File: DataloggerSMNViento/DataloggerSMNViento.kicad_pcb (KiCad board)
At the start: 2 copper layers, 85.7 x 137.2 mm, 37 parts, among them J1 Conn_01x01_Male, J2 Conn_01x01_Male, J3 Conn_01x01_Male, J4 Conn_01x01_Male, Q1 2N7000, Q2 2N7000, Q3 2N7000, U2 w5100_module

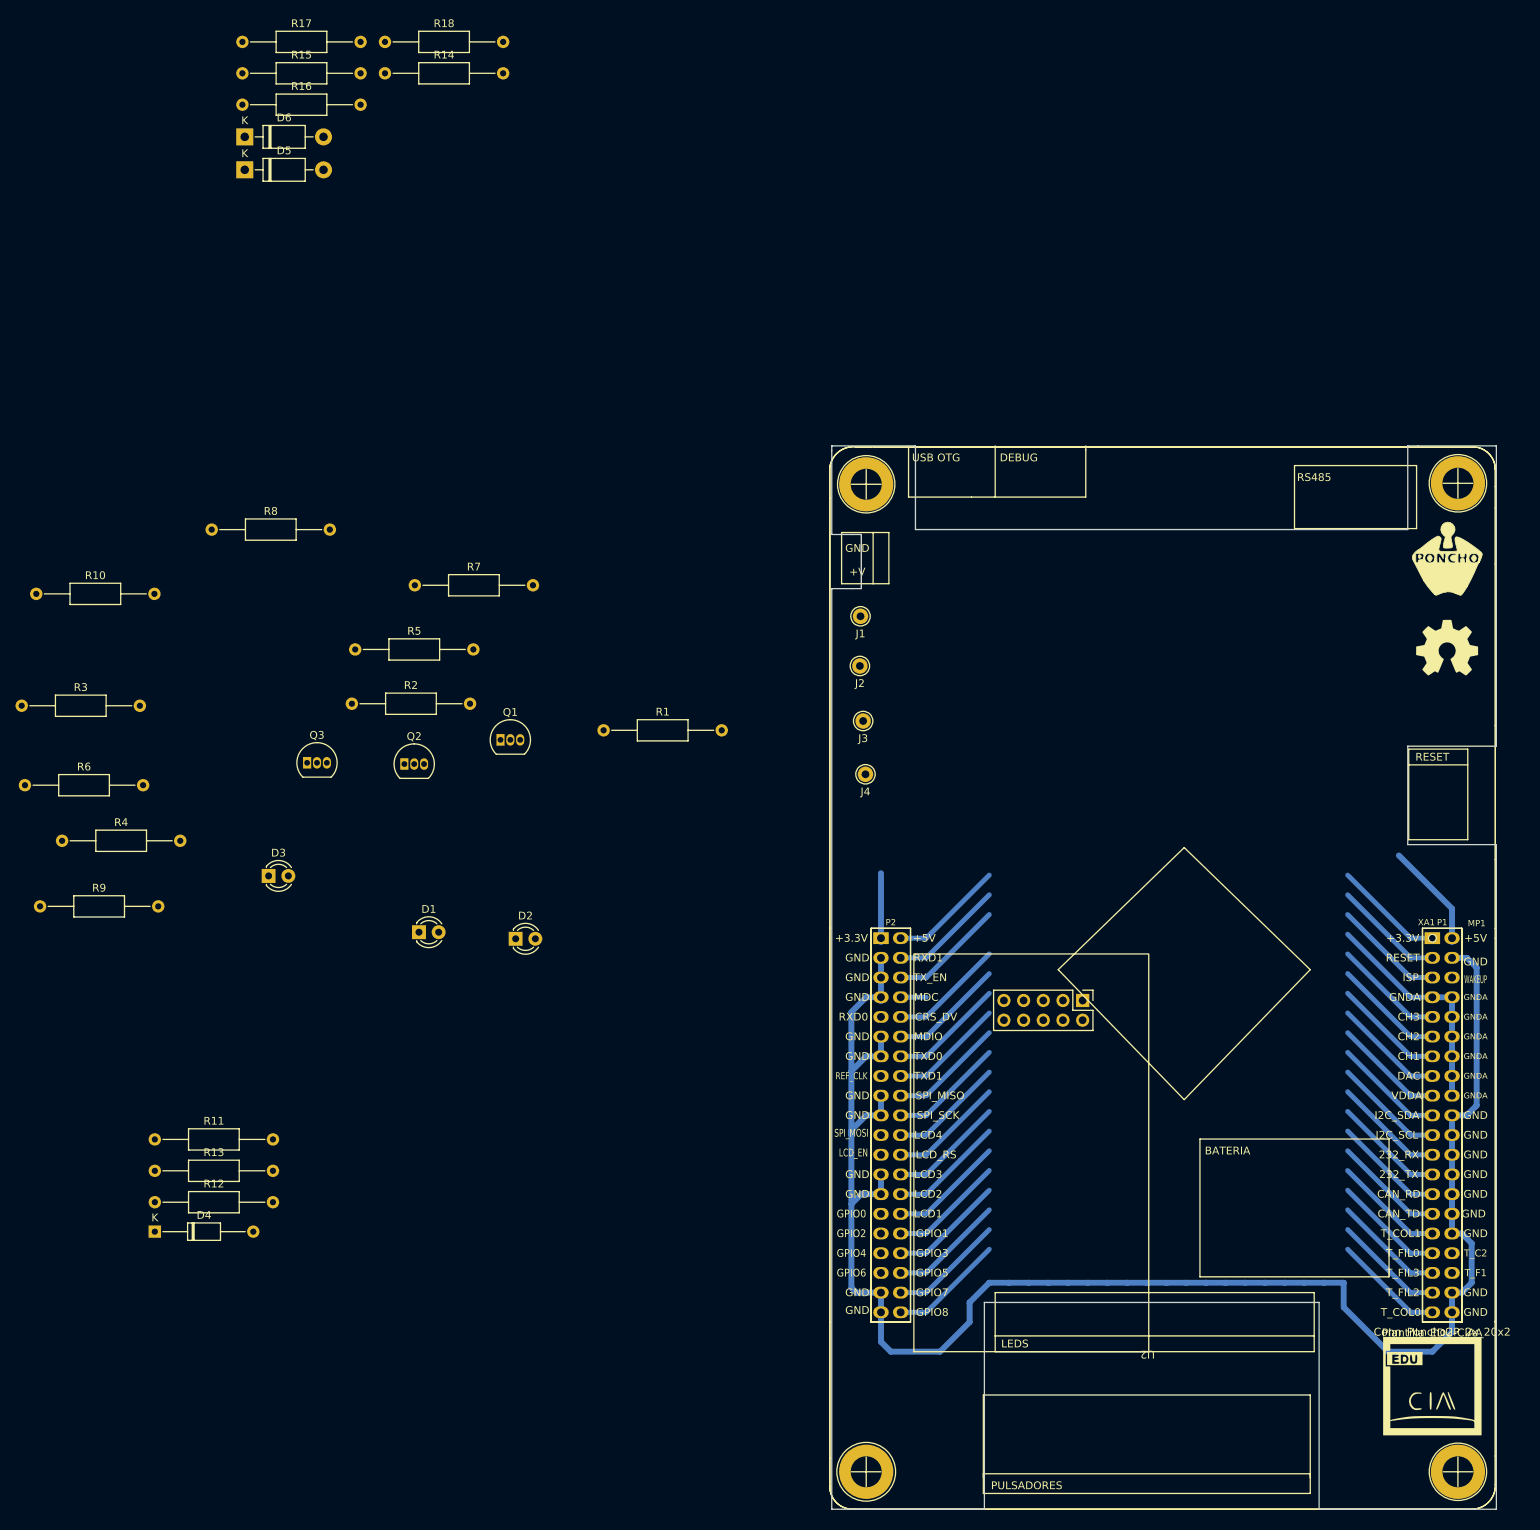
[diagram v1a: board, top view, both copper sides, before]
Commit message: Subo la version v1.0 del PCB del poncho de la tesis
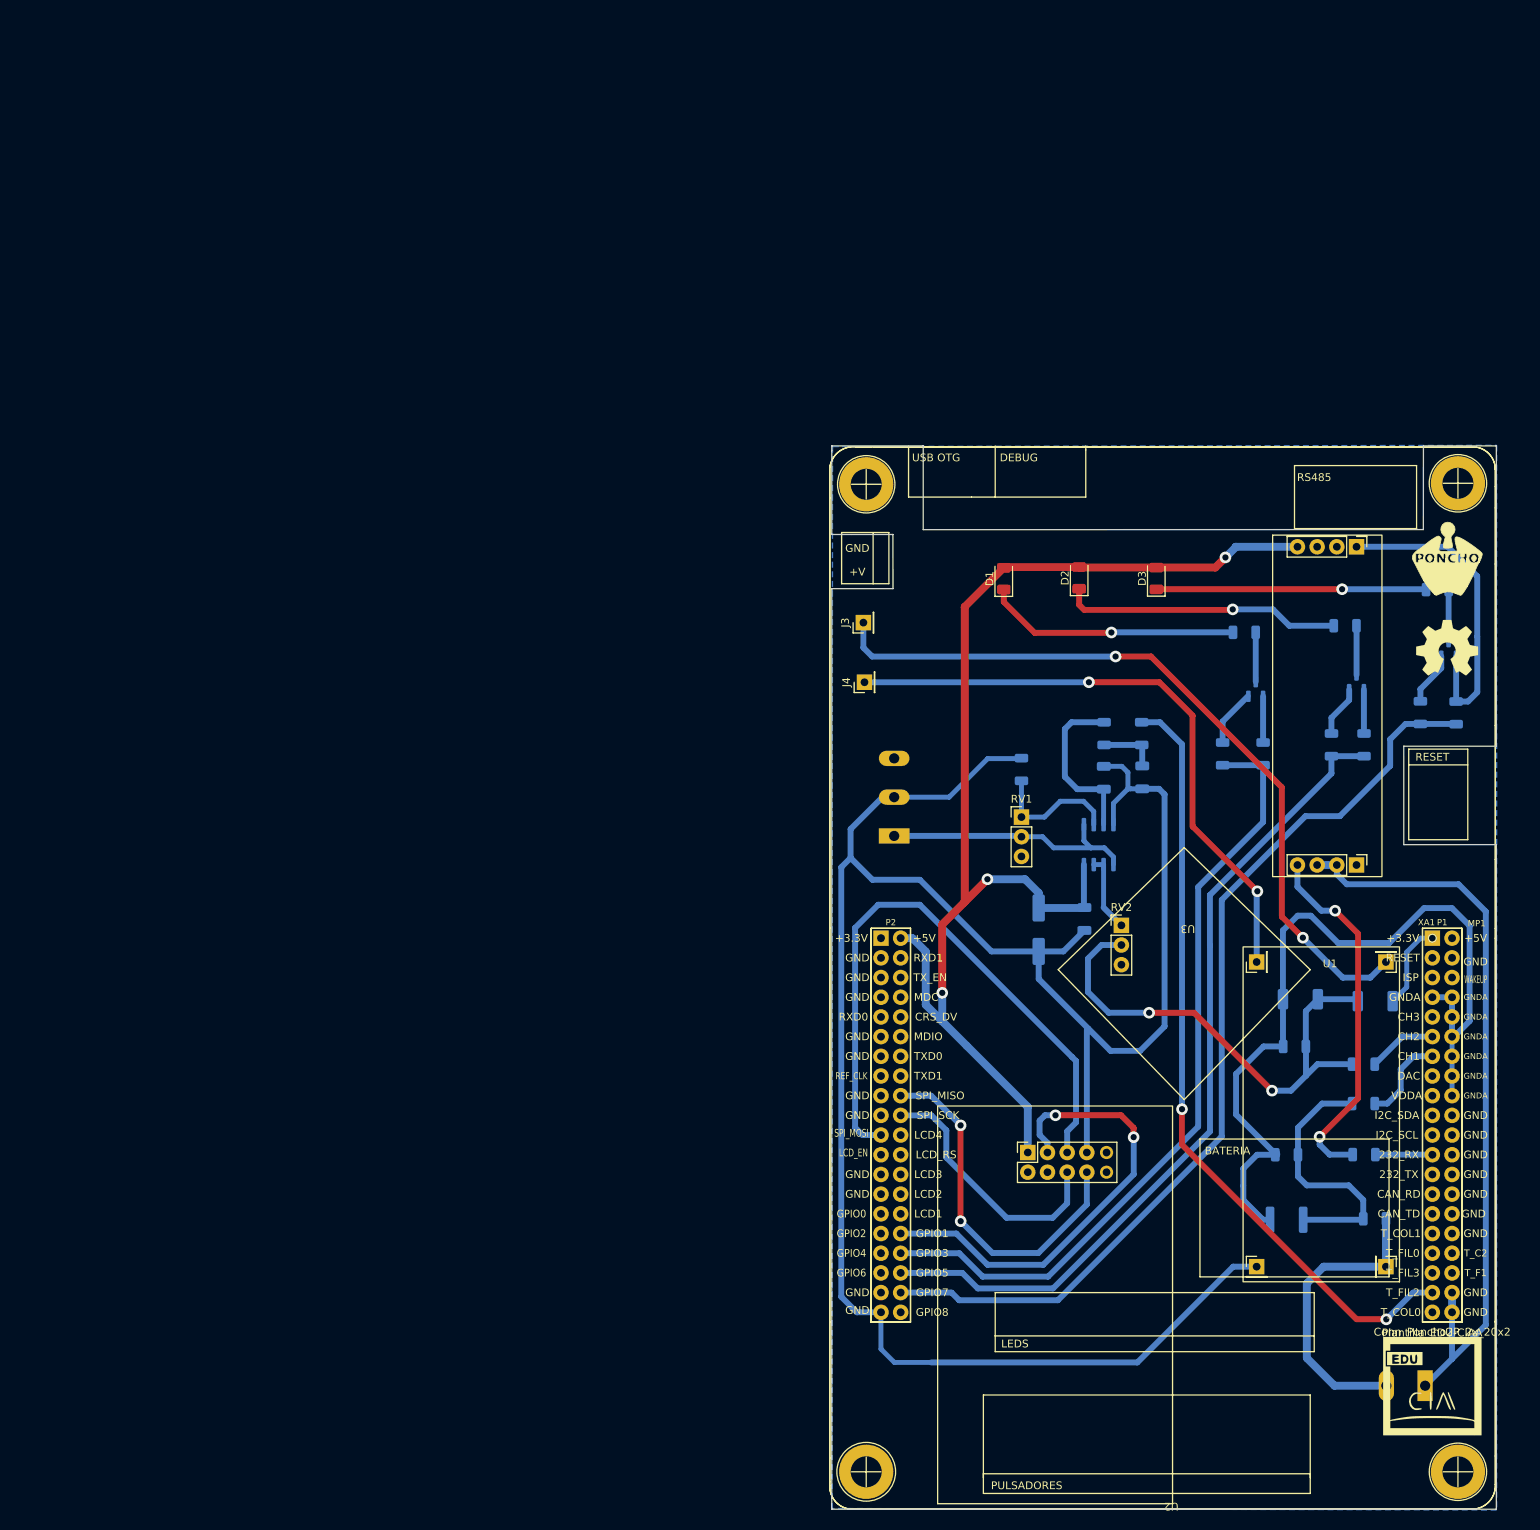
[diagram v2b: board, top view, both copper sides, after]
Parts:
- removed R14: 10k, Resistor_THT:R_Axial_DIN0207_L6.3mm_D2.5mm_P15.24mm_Horizontal
- added C1: 100nF, Capacitor_SMD:C_1206_3216Metric, B.Cu at (113.7, 68.2)
- added C2: 100nF, Capacitor_SMD:C_1206_3216Metric, B.Cu at (108.8, 68.2)
- added C3: 10nF, Capacitor_SMD:C_1206_3216Metric, B.Cu at (106.2, 86.4)
- added C4: C_Polarized 1uF, Capacitor_SMD:CP_Elec_6.3x9.9, B.Cu at (100.3, 87.8)
- added R19: 33k, Resistor_SMD:R_1206_3216Metric, B.Cu at (98.1, 67.1)
- added RV1: R_Filter_Trim 10K, Connector_PinHeader_2.54mm:PinHeader_1x03_P2.54mm_Vertical, F.Cu at (98.1, 73.3)
- added RV2: R_Atenuator_Trim, Connector_PinHeader_2.54mm:PinHeader_1x03_P2.54mm_Vertical, F.Cu at (111.0, 87.2)
- added U1: MAX485E, Modulos:Rs485toTTL, F.Cu at (137.4, 58.3)
- added U3: LM2596S-HW-319-v6_module, Modulos:LM2596_StepDown, F.Cu at (119.6, 87.2)
- added U5: LM358, Package_SO:SO-8_3.9x4.9mm_P1.27mm, B.Cu at (108.1, 76.8)
- D1, D2, D3: footprint LED_THT:LED_D3.0mm -> LED_SMD:LED_1206_3216Metric
- D4: footprint Diode_THT:D_DO-35_SOD27_P12.70mm_Horizontal -> Diode_SMD:D_1812_4532Metric; moved to B.Cu
- D5, D6: footprint Diode_THT:D_DO-41_SOD81_P10.16mm_Horizontal -> Diode_SMD:D_2010_5025Metric; moved to B.Cu
- J1: value Conn_01x01_Male -> Screw_Terminal_01x03; footprint Connector_Pin:Pin_D1.0mm_L10.0mm -> TerminalBlock:TerminalBlock_Altech_AK300-3_P5.00mm; moved to B.Cu
- J2: value Conn_01x01_Male -> Screw_Terminal_01x02; footprint Connector_Pin:Pin_D1.0mm_L10.0mm -> TerminalBlock:TerminalBlock_Altech_AK300-2_P5.00mm; moved to B.Cu
- J3: value Conn_01x01_Male -> Vcc 5V StepDown; footprint Connector_Pin:Pin_D1.0mm_L10.0mm -> Connector_PinHeader_2.54mm:PinHeader_1x01_P2.54mm_Vertical
- J4: value Conn_01x01_Male -> GND StepDowm; footprint Connector_Pin:Pin_D1.0mm_L10.0mm -> Connector_PinHeader_2.54mm:PinHeader_1x01_P2.54mm_Vertical
- Q1, Q2, Q3: footprint Package_TO_SOT_THT:TO-92_Inline -> Package_TO_SOT_SMD:SOT-23; moved to B.Cu
- R1, R10, R11, R12, R13, R18, R2, R3, R4, R5, R6, R7, R8, R9: footprint Resistor_THT:R_Axial_DIN0207_L6.3mm_D2.5mm_P15.24mm_Horizontal -> Resistor_SMD:R_1206_3216Metric; moved to B.Cu
- R15: value 220 -> 33k; footprint Resistor_THT:R_Axial_DIN0207_L6.3mm_D2.5mm_P15.24mm_Horizontal -> Resistor_SMD:R_1206_3216Metric; moved to B.Cu
- R16: value 4k7 -> 10k; footprint Resistor_THT:R_Axial_DIN0207_L6.3mm_D2.5mm_P15.24mm_Horizontal -> Resistor_SMD:R_1206_3216Metric; moved to B.Cu
- R17: value 100k -> 10k; footprint Resistor_THT:R_Axial_DIN0207_L6.3mm_D2.5mm_P15.24mm_Horizontal -> Resistor_SMD:R_1206_3216Metric; moved to B.Cu
- moved R15 184.9 mm to (133.3, 102.9), turned to 180 degrees
- moved R18 182.5 mm to (142.2, 105.2)
- moved D5 181.0 mm to (143.8, 97.0), turned to 180 degrees
- moved R10 180.7 mm to (151.8, 43.9)
- moved R9 179.8 mm to (149.6, 59.8), turned to 90 degrees
- moved D6 175.8 mm to (134.1, 96.8), turned to 180 degrees
- moved R6 168.6 mm to (138.1, 64.0), turned to 90 degrees
- moved R8 162.3 mm to (154.2, 59.8), turned to -90 degrees
- moved R13 157.5 mm to (143.7, 125.1), turned to 180 degrees
- moved R11 156.0 mm to (142.2, 110.2), turned to 180 degrees
- moved R3 155.0 mm to (124.1, 65.1), turned to 90 degrees
- moved R4 154.9 mm to (126.9, 49.5)
- moved Q3 148.0 mm to (153.2, 51.6), turned to 90 degrees
- moved R12 146.1 mm to (132.3, 116.8), turned to 180 degrees
- moved D4 146.0 mm to (132.3, 125.2), turned to 180 degrees
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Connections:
- D4 pad 2: GND -> GNDA
- D6 pad 2: GND -> GNDA
- J1 pad 1: /Conector del Poncho/COL1 -> ADCinVariador
- J2 pad 1: /Conector del Poncho/COL0 -> GNDinVariador
- J3 pad 1: /Conector del Poncho/F3 -> Net-(J3-Pad1)
- J4 pad 1: /Conector del Poncho/F2 -> Net-(J4-Pad1)
- Q1 pad 1: GND -> GNDinVariador
- Q2 pad 1: GND -> GNDinVariador
- Q3 pad 1: GND -> GNDinVariador
- R12 pad 2: GND -> GNDA
- R15 pad 1: Net-(R14-Pad1) -> Net-(D5-Pad2)
- R15 pad 2: Net-(R15-Pad2) -> GNDA
- R16 pad 1: Net-(R15-Pad2) -> /Conector del Poncho/F2
- R16 pad 2: GND -> Net-(C1-Pad1)
- R17 pad 1: Net-(R14-Pad1) -> Net-(C1-Pad1)
- R17 pad 2: Net-(D5-Pad2) -> Net-(C2-Pad1)
- R2 pad 1: GND -> GNDinVariador
- R2 pad 2: /Conector del Poncho/GPIO2 -> /Conector del Poncho/GPIO3
- R3 pad 1: /Conector del Poncho/GPIO2 -> /Conector del Poncho/GPIO3
- R5 pad 1: GND -> GNDinVariador
- R5 pad 2: /Conector del Poncho/GPIO4 -> /Conector del Poncho/GPIO5
- R6 pad 1: /Conector del Poncho/GPIO4 -> /Conector del Poncho/GPIO5
- R8 pad 1: GND -> GNDinVariador
- R8 pad 2: /Conector del Poncho/GPIO6 -> /Conector del Poncho/GPIO7
- R9 pad 1: /Conector del Poncho/GPIO6 -> /Conector del Poncho/GPIO7
- U2 pad 10: GND -> unconnected-(U2-Pad10)
- U2 pad 2: /Conector del Poncho/GPIO0 -> /Conector del Poncho/GPIO1
- U2 pad 4: GND -> GNDinVariador
- XA1 pad 2: +5V -> unconnected-(XA1-Pad2)
- XA1 pad 20: GND -> unconnected-(XA1-Pad20)
- XA1 pad 22: GND -> unconnected-(XA1-Pad22)
- XA1 pad 24: GND -> unconnected-(XA1-Pad24)
- XA1 pad 26: GND -> unconnected-(XA1-Pad26)
- XA1 pad 28: GND -> unconnected-(XA1-Pad28)
- XA1 pad 30: GND -> unconnected-(XA1-Pad30)
- XA1 pad 31: /Conector del Poncho/COL1 -> unconnected-(XA1-Pad31)
- XA1 pad 32: GND -> unconnected-(XA1-Pad32)
- XA1 pad 35: /Conector del Poncho/F3 -> unconnected-(XA1-Pad35)
- XA1 pad 38: GND -> GNDinVariador
- XA1 pad 39: /Conector del Poncho/COL0 -> unconnected-(XA1-Pad39)
- XA1 pad 4: GND -> unconnected-(XA1-Pad4)
- XA1 pad 40: GND -> GNDinVariador
- XA1 pad 41: +3.3V -> unconnected-(XA1-Pad41)
- XA1 pad 43: GND -> unconnected-(XA1-Pad43)
- XA1 pad 45: GND -> unconnected-(XA1-Pad45)
- XA1 pad 47: GND -> unconnected-(XA1-Pad47)
- XA1 pad 51: GND -> unconnected-(XA1-Pad51)
- XA1 pad 53: GND -> unconnected-(XA1-Pad53)
- XA1 pad 57: GND -> unconnected-(XA1-Pad57)
- XA1 pad 59: GND -> unconnected-(XA1-Pad59)
- XA1 pad 65: GND -> unconnected-(XA1-Pad65)
- XA1 pad 67: GND -> unconnected-(XA1-Pad67)
- XA1 pad 69: /Conector del Poncho/GPIO0 -> unconnected-(XA1-Pad69)
- XA1 pad 71: /Conector del Poncho/GPIO2 -> unconnected-(XA1-Pad71)
- XA1 pad 72: unconnected-(XA1-Pad72) -> /Conector del Poncho/GPIO1
- XA1 pad 73: /Conector del Poncho/GPIO4 -> unconnected-(XA1-Pad73)
- XA1 pad 74: unconnected-(XA1-Pad74) -> /Conector del Poncho/GPIO3
- XA1 pad 75: /Conector del Poncho/GPIO6 -> unconnected-(XA1-Pad75)
- XA1 pad 76: unconnected-(XA1-Pad76) -> /Conector del Poncho/GPIO5
- XA1 pad 77: GND -> unconnected-(XA1-Pad77)
- XA1 pad 78: unconnected-(XA1-Pad78) -> /Conector del Poncho/GPIO7
- XA1 pad 79: GND -> GNDinVariador
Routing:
- net GNDinVariador: track 0.00 -> 425.5 mm
- net GND: track 219.6 -> 0.00 mm
- net +5V: track 28.8 -> 161.3 mm, vias 0 -> 3
- net /Conector del Poncho/GPIO7: track 0.00 -> 122.7 mm
- net /Conector del Poncho/GPIO5: track 0.00 -> 108.2 mm
- net /Conector del Poncho/GPIO3: track 0.00 -> 103.0 mm
- net Net-(J3-Pad1): track 0.00 -> 98.9 mm, vias 0 -> 2
- net /Conector del Poncho/F2: track 14.3 -> 101.1 mm, vias 0 -> 2
- net /Conector del Poncho/MOSI: track 0.00 -> 79.9 mm
- net Net-(J4-Pad1): track 0.00 -> 79.4 mm, vias 0 -> 2
- net GNDA: track 29.5 -> 108.2 mm
- net Net-(D5-Pad2): track 0.00 -> 65.9 mm, vias 0 -> 2
- net /Conector del Poncho/GPIO1: track 0.00 -> 60.2 mm, vias 0 -> 2
- net Net-(R1-Pad2): track 0.00 -> 47.2 mm, vias 0 -> 2
- net +12V: track 0.00 -> 38.8 mm
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- added copper zone on B.Cu, net GNDinVariador
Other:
- outline, holes or cut-outs redrawn

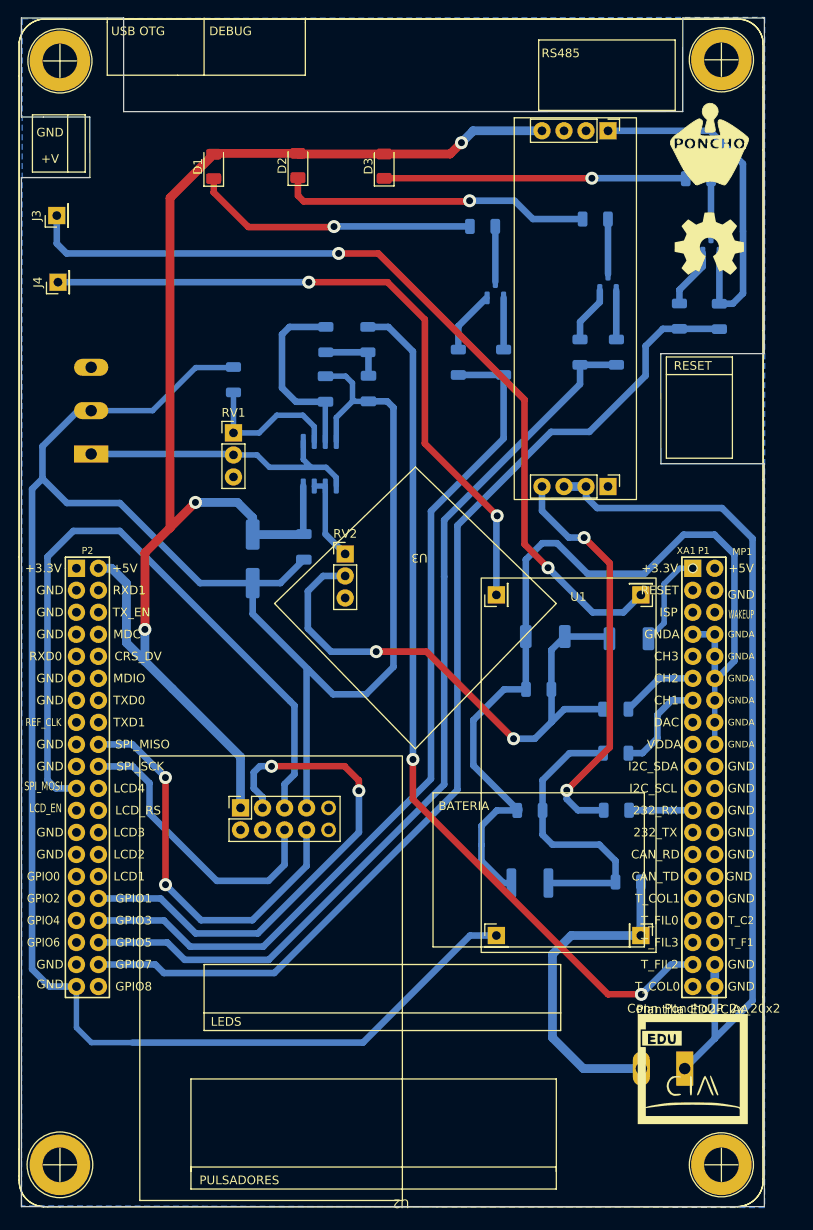
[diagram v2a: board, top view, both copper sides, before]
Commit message: Se cambio la alimentacion de los modulos por el stepDown
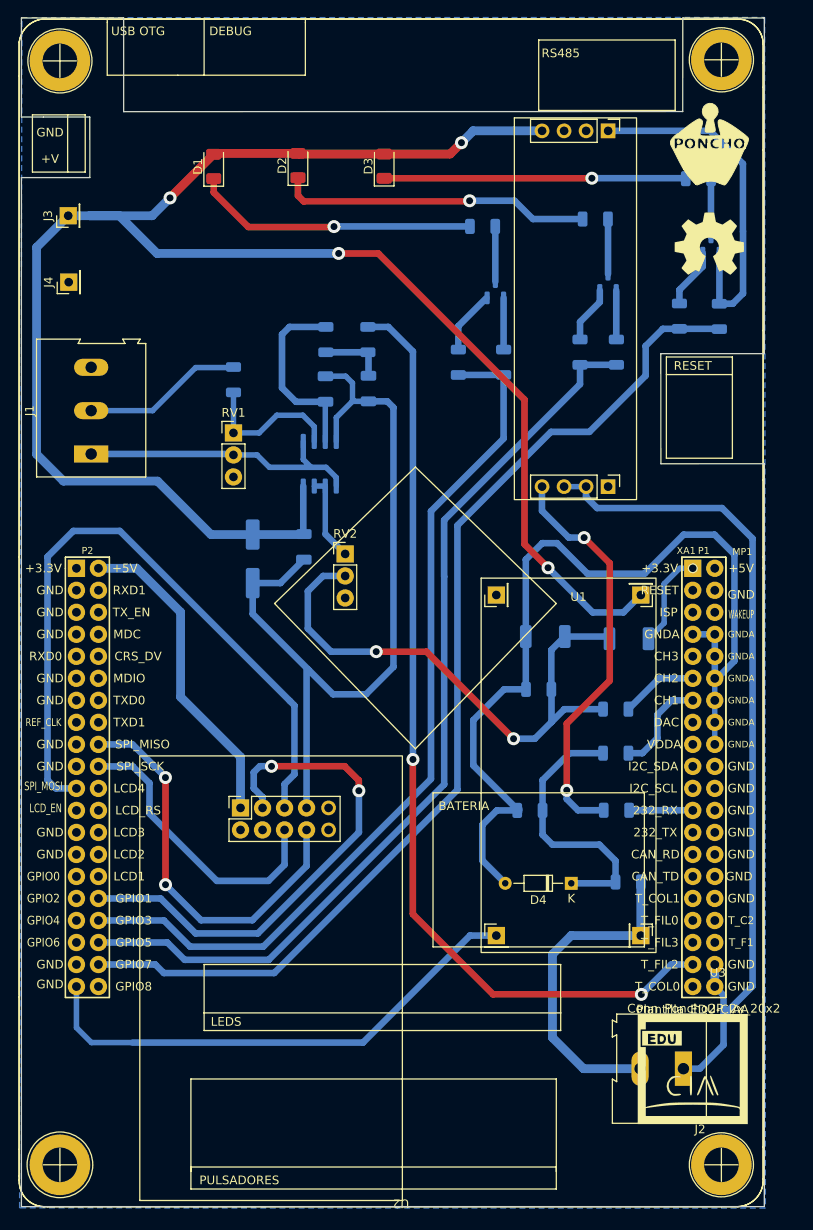
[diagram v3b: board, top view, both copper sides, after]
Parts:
- D4: footprint Diode_SMD:D_1812_4532Metric -> Diode_THT:D_DO-34_SOD68_P7.62mm_Horizontal; moved to F.Cu
- J1, J2: moved to F.Cu
- J3: value Vcc 5V StepDown -> Vcc 5V SD
- J4: value GND StepDowm -> GND SD
- moved U3 59.8 mm to (154.0, 136.1), turned to 0 degrees
- moved D4 4.78 mm to (137.1, 125.2)
- moved J3 1.32 mm to (79.1, 48.2)
- moved J4 1.24 mm to (79.1, 55.9)
- moved J2 0.15 mm to (150.1, 146.6)
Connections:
- C3 pad 1: +5V -> +5VP
- C4 pad 1: +5V -> +5VP
- D1 pad 2: +5V -> +5VP
- D2 pad 2: +5V -> +5VP
- D3 pad 2: +5V -> +5VP
- J3 pad 1: Net-(J3-Pad1) -> +5VP
- J4 pad 1: Net-(J4-Pad1) -> GNDinVariador
- U1 pad 8: +5V -> +5VP
- U3 pad 3: Net-(J4-Pad1) -> unconnected-(U3-Pad3)
- U3 pad 4: Net-(J3-Pad1) -> +5VP
- U5 pad 8: +5V -> +5VP
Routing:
- net +5VP: track 0.00 -> 221.3 mm, vias 0 -> 4
- net +5V: track 161.3 -> 37.0 mm, vias 3 -> 0
- net GNDinVariador: track 425.5 -> 321.1 mm
- net Net-(J3-Pad1): track 98.9 -> 0.00 mm, vias 2 -> 0
- net Net-(J4-Pad1): track 79.4 -> 0.00 mm, vias 2 -> 0
- net /Conector del Poncho/F2: track 101.1 -> 108.9 mm
- net Net-(D4-Pad1): track 34.5 -> 32.0 mm
- net GNDA: track 108.2 -> 107.3 mm
